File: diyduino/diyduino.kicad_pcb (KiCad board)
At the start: 2 copper layers, 22 parts, among them U1 ATMEGA328-PU, U2 L7805, Y1 16MHz

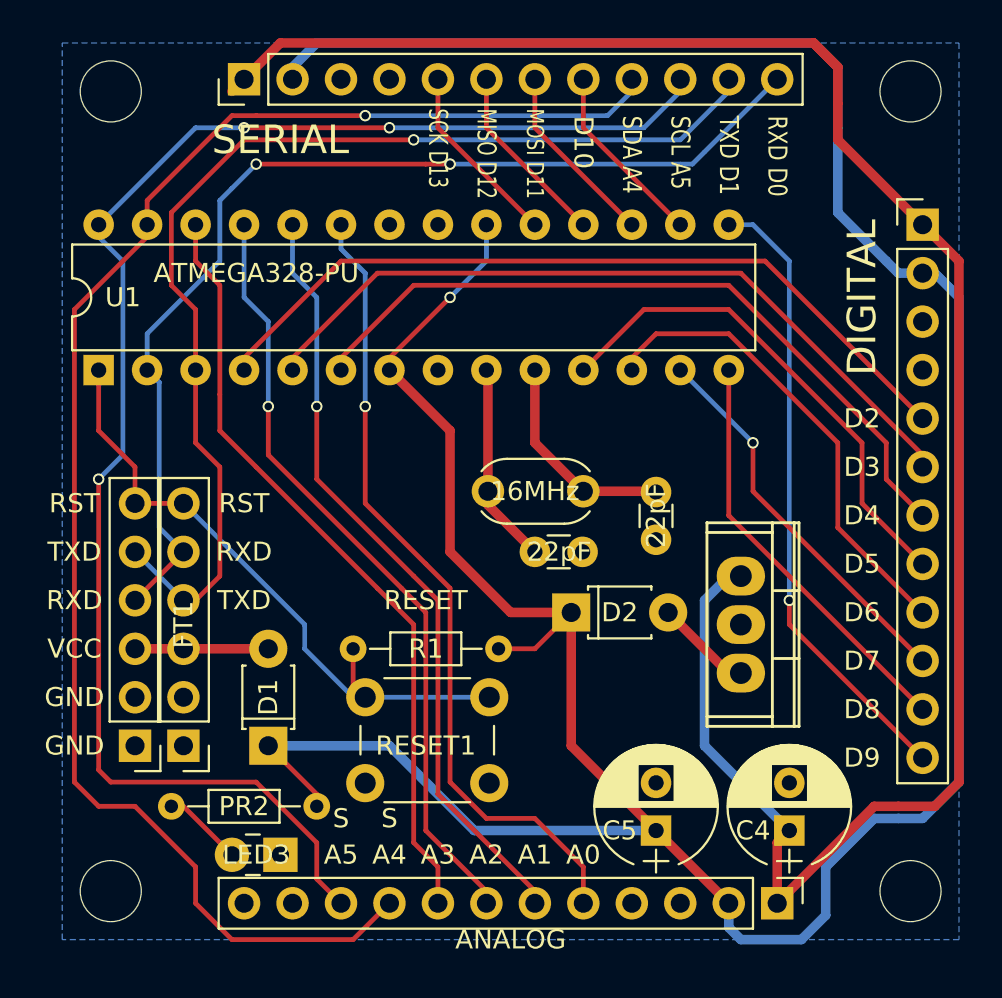
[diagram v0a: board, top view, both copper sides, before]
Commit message: More work to ensure there are no errors from KiCAD's schematic checker. Fixed the multiplexer module, so that all 7 slaves will work (only 6 were working, due to a missing VCC to the "Next Output").
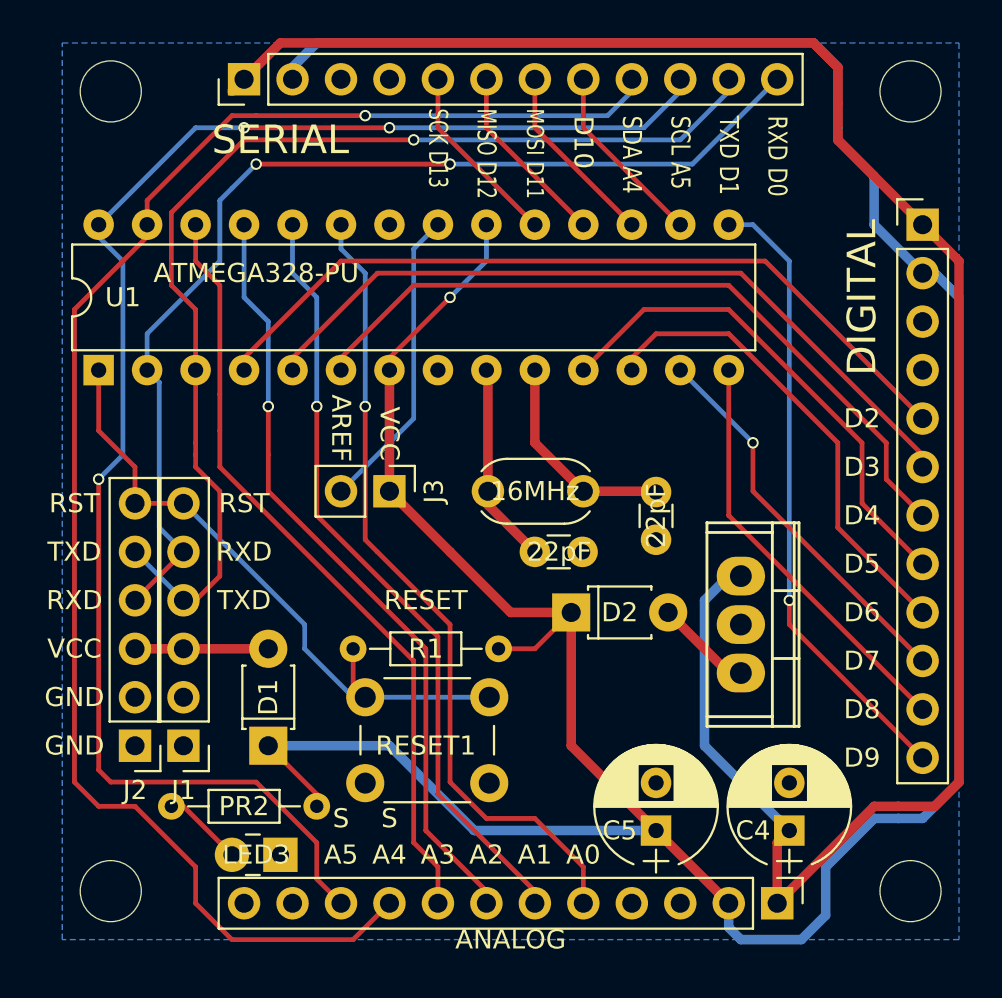
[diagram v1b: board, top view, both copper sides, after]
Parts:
- removed FT1, FT2: FTDI, Pin_Headers:Pin_Header_Straight_1x06_Pitch2.54mm
- added J1: ICSP, Pin_Headers:Pin_Header_Straight_1x06_Pitch2.54mm, F.Cu at (116.2, 69.2)
- added J2: ICSP, Pin_Headers:Pin_Header_Straight_1x06_Pitch2.54mm, F.Cu at (113.7, 69.2)
- added J3: Conn_01x02, Pin_Headers:Pin_Header_Straight_1x02_Pitch2.54mm, F.Cu at (127.0, 55.9)
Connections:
- net Earth renamed /GND
- U1 pad 21: (no net) -> /AREF
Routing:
- net /AREF: track 0.00 -> 16.1 mm
- net /VCC: track 167.9 -> 167.1 mm
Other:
- board text added: "AREF"
